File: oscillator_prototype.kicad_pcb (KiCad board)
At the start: 2 copper layers, 99 parts, among them J1 shark fin, J2 Exp FM, J3 1v/oct, J4 Triangle, J5 Pulse, J6 Sync, J7 Eurorack power, J8 Linear FM, J9 PWM, Q1 MMBT3904, Q2 MMBT3906, Q3 BC857BS, Q4 MMBT3904, Q5 MMBT3904, SW1 Sync Mode, SW2 Audio/LFO, U1 LT1013, U2 TL074, U3 LM13700, U4 LM311, U5 LM311, U6 DG418, U7 LM311, U8 TL072

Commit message: Switch to SMT resistors/caps/diodes (mostly)
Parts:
- C1: footprint Capacitor_THT:C_Disc_D5.0mm_W2.5mm_P5.00mm -> Capacitor_SMD:C_0603_1608Metric_Pad1.08x0.95mm_HandSolder
- C10, C11, C12, C13, C14, C15, C16, C17, C19, C20, C21, C22, C23, C24, C25, C26, C3, C4, C5, C7, C8: footprint Capacitor_THT:C_Disc_D5.0mm_W2.5mm_P5.00mm -> Capacitor_SMD:C_0805_2012Metric_Pad1.18x1.45mm_HandSolder
- D1, D2, D3: footprint Diode_THT:D_DO-35_SOD27_P7.62mm_Horizontal -> Diode_SMD:D_0805_2012Metric_Pad1.15x1.40mm_HandSolder
- JP1: moved to B.Cu
- R1, R10, R11, R12, R13, R14, R15, R16, R17, R18, R19, R2, R20, R21, R22, R23, R24, R25, R26, R27, R28, R29, R3, R30, R31, R32, R33, R34, R5, R6, R7, R8, R9: footprint Resistor_THT:R_Axial_DIN0204_L3.6mm_D1.6mm_P5.08mm_Horizontal -> Resistor_SMD:R_0805_2012Metric_Pad1.20x1.40mm_HandSolder
- R4: footprint Resistor_THT:R_Axial_DIN0207_L6.3mm_D2.5mm_P7.62mm_Horizontal -> Resistor_THT:R_Axial_DIN0204_L3.6mm_D1.6mm_P5.08mm_Horizontal
- moved C5 231.3 mm to (46.2, 89.0)
- moved R28 221.7 mm to (55.5, 89.5)
- moved R24 205.7 mm to (50.2, 89.5)
- moved R17 192.4 mm to (97.8, 145.5)
- moved R33 174.4 mm to (99.2, 117.5)
- moved R19 172.7 mm to (92.8, 130.5)
- moved R34 151.3 mm to (107.0, 118.8)
- moved R2 150.5 mm to (116.8, 118.8)
- moved R5 144.8 mm to (117.8, 138.0)
- moved R32 138.1 mm to (112.0, 118.8)
- moved R14 120.0 mm to (150.8, 89.8)
- moved R16 114.9 mm to (118.0, 145.2)
- moved R23 110.0 mm to (138.8, 141.8)
- moved R26 109.7 mm to (166.5, 137.5)
- moved R15 108.0 mm to (163.0, 67.5)
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
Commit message: Complete layout
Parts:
- removed C16, C17, C25, C26, C7, C8: 100n, Capacitor_SMD:C_0805_2012Metric_Pad1.18x1.45mm_HandSolder
- removed J2: Exp FM, kicad_libraries:Jack_3.5mm_QingPu_WQP-PJ398SM_Vertical_CircularHoles-translated
- removed J5: Pulse, kicad_libraries:Jack_3.5mm_QingPu_WQP-PJ398SM_Vertical_CircularHoles-translated
- removed R34: 100k, Resistor_SMD:R_0805_2012Metric_Pad1.20x1.40mm_HandSolder
- removed RV8: B100k, kicad_libraries:Potentiometer_Alpha_RD901F-40-00D_Single_Vertical-translated
- removed RV9: 100k, kicad_libraries:Potentiometer_Alpha_RD901F-40-00D_Single_Vertical-translated
- removed SW2: Audio/LFO, ljwall-kicad-footprints:Dailywell_sub-mini_toggle_DPDT
- added D6: 1N4148, Diode_SMD:D_0805_2012Metric_Pad1.15x1.40mm_HandSolder, F.Cu at (103.0, 115.8)
- added D7: 1N4148, Diode_SMD:D_0805_2012Metric_Pad1.15x1.40mm_HandSolder, F.Cu at (100.8, 115.8)
- added D8: 1N4148, Diode_SMD:D_0805_2012Metric_Pad1.15x1.40mm_HandSolder, F.Cu at (107.8, 106.8)
- added D9: 1N4148, Diode_SMD:D_0805_2012Metric_Pad1.15x1.40mm_HandSolder, F.Cu at (105.5, 106.8)
- added J10: Conn_01x06_Male, Connector_PinHeader_2.54mm:PinHeader_1x06_P2.54mm_Vertical, F.Cu at (97.8, 102.0)
- added J11: Conn_01x06_Female, Connector_PinHeader_2.54mm:PinHeader_1x06_P2.54mm_Vertical, B.Cu at (83.0, 107.0)
- added J12: Conn_01x06_Male, Connector_PinHeader_2.54mm:PinHeader_1x06_P2.54mm_Vertical, F.Cu at (133.0, 107.0)
- added J13: Conn_01x06_Female, Connector_PinHeader_2.54mm:PinHeader_1x06_P2.54mm_Vertical, B.Cu at (47.0, 48.0)
- added J14: Conn_01x06_Male, Connector_PinHeader_2.54mm:PinHeader_1x06_P2.54mm_Vertical, F.Cu at (97.0, 48.0)
- added TP1: vref, TestPoint:TestPoint_Pad_D2.0mm, B.Cu at (109.8, 114.0)
- C1: value C_Small -> 1n; footprint Capacitor_SMD:C_0603_1608Metric_Pad1.08x0.95mm_HandSolder -> Capacitor_SMD:C_0805_2012Metric_Pad1.18x1.45mm_HandSolder
- C5: value 10n -> 100n
- C6: value 470n (polyester) -> 100n; footprint Capacitor_THT:C_Rect_L7.2mm_W3.5mm_P5.00mm_FKS2_FKP2_MKS2_MKP2 -> Capacitor_SMD:C_0805_2012Metric_Pad1.18x1.45mm_HandSolder
- J7: footprint Connector_IDC:IDC-Header_2x05_P2.54mm_Vertical -> Connector_IDC:IDC-Header_2x05_P2.54mm_Horizontal; moved to F.Cu
- J9: value PWM -> Conn_01x06_Female; footprint kicad_libraries:Jack_3.5mm_QingPu_WQP-PJ398SM_Vertical_CircularHoles-translated -> Connector_PinHeader_2.54mm:PinHeader_1x06_P2.54mm_Vertical; moved to B.Cu
- R10, R14: value R_Small_US -> 100k
- R17: value 20k -> 120k
- R19: value 1k -> 3k6
- R24: value 1k -> 10k
- R28: value 1k -> 4k7
- R3: value R_Small_US -> 68k
- R32: value 100k -> 10k
- R33: value 100k -> 4k7
- R6: value R_Small_US -> 680k
- RV1, RV2: value 100k -> 50k
- RV4: value 100k -> 2k; footprint kicad_libraries:Potentiometer_Alpha_RD901F-40-00D_Single_Vertical-translated -> Potentiometer_THT:Potentiometer_Bourns_3266X_Horizontal
- U1: value LT1013 -> LT1013-SOIC
- U5: value LM311 -> LT1013-SOIC
- U8: value TL072 -> LM336Z-5.0; footprint Package_SO:SOIC-8_3.9x4.9mm_P1.27mm -> Package_TO_SOT_THT:TO-92_Inline
- moved C11 143.5 mm to (101.8, 130.5), turned to 270 degrees
- moved C24 139.3 mm to (96.2, 125.8), turned to 90 degrees
- moved C19 127.6 mm to (104.0, 87.0), turned to 90 degrees
- moved C13 119.8 mm to (98.0, 78.0), turned to 270 degrees
- moved C23 116.3 mm to (113.2, 79.0), turned to 180 degrees
- moved C15 112.1 mm to (106.8, 64.0), turned to 90 degrees
- moved U7 111.8 mm to (102.0, 79.8), turned to 90 degrees
- moved C21 109.9 mm to (119.8, 61.2)
- moved D5 109.3 mm to (132.2, 133.2), turned to 90 degrees
- moved D4 107.8 mm to (128.5, 123.0), turned to 270 degrees
- moved R10 104.9 mm to (66.5, 70.2)
- moved C22 102.7 mm to (126.5, 72.8), turned to 270 degrees
- moved C14 101.2 mm to (117.0, 71.0), turned to 180 degrees
- moved U8 101.1 mm to (105.8, 111.5)
- moved D2 100.2 mm to (101.0, 96.2), turned to 270 degrees
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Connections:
- net /SC_b renamed Net-(C4-Pad1)
- C15 pad 1: +12V -> GND
- C15 pad 2: GND -> -12V
- C4 pad 2: /SC_a -> sync_m
- C5 pad 1: Net-(C5-Pad1) -> +12V
- C5 pad 2: /SC_a -> GND
- C6 pad 1: Net-(C6-Pad1) -> +12V
- C6 pad 2: /TC_b -> GND
- J1 pad S: GND -> GND_f
- J1 pad T: Net-(J1-PadT) -> saw_f
- J3 pad S: GND -> GND_f
- J3 pad T: Net-(J3-PadT) -> v_per_oct_f
- J3 pad TN: GND -> GND_f
- J4 pad S: GND -> GND_f
- J4 pad T: Net-(J4-PadT) -> tri_f
- J6 pad S: GND -> GND_f
- J6 pad T: /SC_a -> sync_f
- J6 pad TN: GND -> GND_f
- J8 pad S: GND -> GND_f
- J8 pad TN: GND -> GND_f
- R10 pad 1: Net-(C1-Pad2) -> 5V_f
- R14 pad 2: Net-(J3-PadT) -> v_per_oct_m
- R16 pad 2: Net-(J4-PadT) -> tri_m
- R17 pad 1: Net-(R17-Pad1) -> Net-(C1-Pad2)
- R17 pad 2: +5V -> -5V
- R19 pad 1: Net-(R19-Pad1) -> +12V
- R19 pad 2: Net-(J5-PadT) -> Net-(D6-Pad2)
- R23 pad 1: Net-(R23-Pad1) -> switch_b_m
- R24 pad 1: /SC_a -> Net-(R24-Pad1)
- R24 pad 2: Net-(R24-Pad2) -> -5V
- R28 pad 1: /TC_b -> Net-(D7-Pad1)
- R3 pad 2: Net-(R3-Pad2) -> coarse_m
- R30 pad 1: /TC_b -> /TC_a
- R31 pad 2: Net-(R31-Pad2) -> lin_fm_m
- R32 pad 1: Net-(R32-Pad1) -> Net-(D6-Pad2)
- R32 pad 2: Net-(R32-Pad2) -> Net-(R24-Pad1)
- R33 pad 1: Net-(R32-Pad2) -> Net-(R33-Pad1)
- R5 pad 2: Net-(J1-PadT) -> saw_m
- R6 pad 2: Net-(R6-Pad2) -> fine_m
- RV1 pad 1: -5V -> GND_f
- RV1 pad 2: Net-(R3-Pad2) -> coarse_f
- RV1 pad 3: +5V -> 5V_f
- RV2 pad 1: GND -> GND_f
- RV2 pad 2: Net-(R6-Pad2) -> fine_f
- RV2 pad 3: +5V -> Net-(R10-Pad2)
- RV4 pad 1: Net-(J2-PadT) -> Net-(R33-Pad1)
- RV4 pad 2: Net-(R10-Pad2) -> Net-(RV4-Pad2)
- RV4 pad 3: GND -> Net-(R28-Pad2)
- RV5 pad 1: -5V -> Net-(R20-Pad2)
- RV5 pad 3: Net-(R20-Pad2) -> -5V
- RV7 pad 1: GND -> GND_f
- RV7 pad 2: Net-(R31-Pad2) -> lin_fm_f
- SW1 pad 1: Net-(R23-Pad1) -> switch_b_f
- SW1 pad 2: Net-(SW1-Pad2) -> switch_a_f
- U1 pad 1: Net-(C3-Pad1) -> GND
- U1 pad 2: Net-(C3-Pad2) -> -12V
- U1 pad 4: -12V -> Net-(C3-Pad2)
- U1 pad 5: GND -> Net-(C3-Pad1)
- U1 pad 6: Net-(C1-Pad2) -> +12V
- U1 pad 8: +12V -> Net-(C1-Pad2)
- U2 pad 1: Net-(R32-Pad1) -> Net-(R16-Pad1)
- U2 pad 12: /TC_b -> GND
- U2 pad 13: Net-(R16-Pad1) -> /TC_a
- U2 pad 14: Net-(R16-Pad1) -> /TC_b
- U2 pad 2: Net-(R32-Pad2) -> Net-(R16-Pad1)
- U2 pad 3: GND -> /TC_b
- U2 pad 5: Net-(R17-Pad1) -> GND
- U2 pad 6: Net-(R19-Pad1) -> Net-(U2-Pad6)
- U2 pad 7: Net-(R19-Pad1) -> Net-(U2-Pad6)
- U3 pad 1: Net-(Q2-Pad3) -> Net-(Q3-Pad6)
- U3 pad 10: +12V -> Net-(U3-Pad10)
- U3 pad 12: /TC_a -> Net-(R1-Pad2)
- U3 pad 16: Net-(Q3-Pad6) -> Net-(Q2-Pad3)
- U3 pad 5: Net-(R1-Pad2) -> /TC_a
- U3 pad 7: +12V -> Net-(U3-Pad7)
- U3 pad 8: +12V -> Net-(U3-Pad7)
- U3 pad 9: +12V -> Net-(U3-Pad10)
- U5 pad 1: -5V -> Net-(D6-Pad2)
- U5 pad 2: /TC_b -> -12V
- U5 pad 3: Net-(R32-Pad1) -> GND
- U5 pad 4: -12V -> Net-(R24-Pad1)
- U5 pad 5: Net-(U5-Pad5) -> -5V
- U5 pad 6: Net-(U5-Pad6) -> +12V
- U5 pad 7: Net-(R17-Pad1) -> +5V
- U5 pad 8: +12V -> +5V
- U6 pad 1: /TC_a -> /TC_b
- U6 pad 6: Net-(R23-Pad1) -> switch_b_m
- U7 pad 1: Net-(SW1-Pad2) -> switch_a_m
- U8 pad 1: /TC_b -> Net-(RV4-Pad2)
- U8 pad 2: /TC_a -> Net-(D6-Pad2)
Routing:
- net -12V: track 0.00 -> 270.8 mm, vias 0 -> 8
- net +12V: track 0.00 -> 231.9 mm, vias 0 -> 8
- net +5V: track 0.00 -> 105.5 mm, vias 0 -> 6
- net -5V: track 0.00 -> 103.9 mm, vias 0 -> 4
- net /TC_b: track 0.00 -> 77.3 mm
- net lin_fm_f: track 0.00 -> 76.5 mm, vias 0 -> 2
- net 5V_f: track 0.00 -> 58.8 mm
- net coarse_f: track 0.00 -> 58.6 mm
- net tri_f: track 0.00 -> 54.2 mm, vias 0 -> 4
- net saw_f: track 0.00 -> 49.9 mm, vias 0 -> 4
- net switch_a_f: track 0.00 -> 44.8 mm
- net /TC_a: track 0.00 -> 42.3 mm
- net v_per_oct_f: track 0.00 -> 42.3 mm
- net switch_b_f: track 0.00 -> 39.5 mm
- net Net-(C1-Pad2): track 0.00 -> 35.0 mm, vias 0 -> 1
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- added copper zone on B.Cu, net GND
- added copper zone on F.Cu, net GND
- added copper zone on B.Cu, net GND_f
- added copper zone on F.Cu, net GND_f
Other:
- board outline added: 98.5 x 117 mm
- board text added: "+12V"
- board text added: "-12V"
- board text added: "GND"
- board text added: "Oscillator Prototype 1"
- board text added: "bridge for init trim"
- board text added: "bridge to operate"
- board text added: "hf trim"
- board text added: "init"
- board text added: "red stripe"
- board text added: "v/oct trim"
- board text added: "vref (5v)"
- board text added: "vref trim"

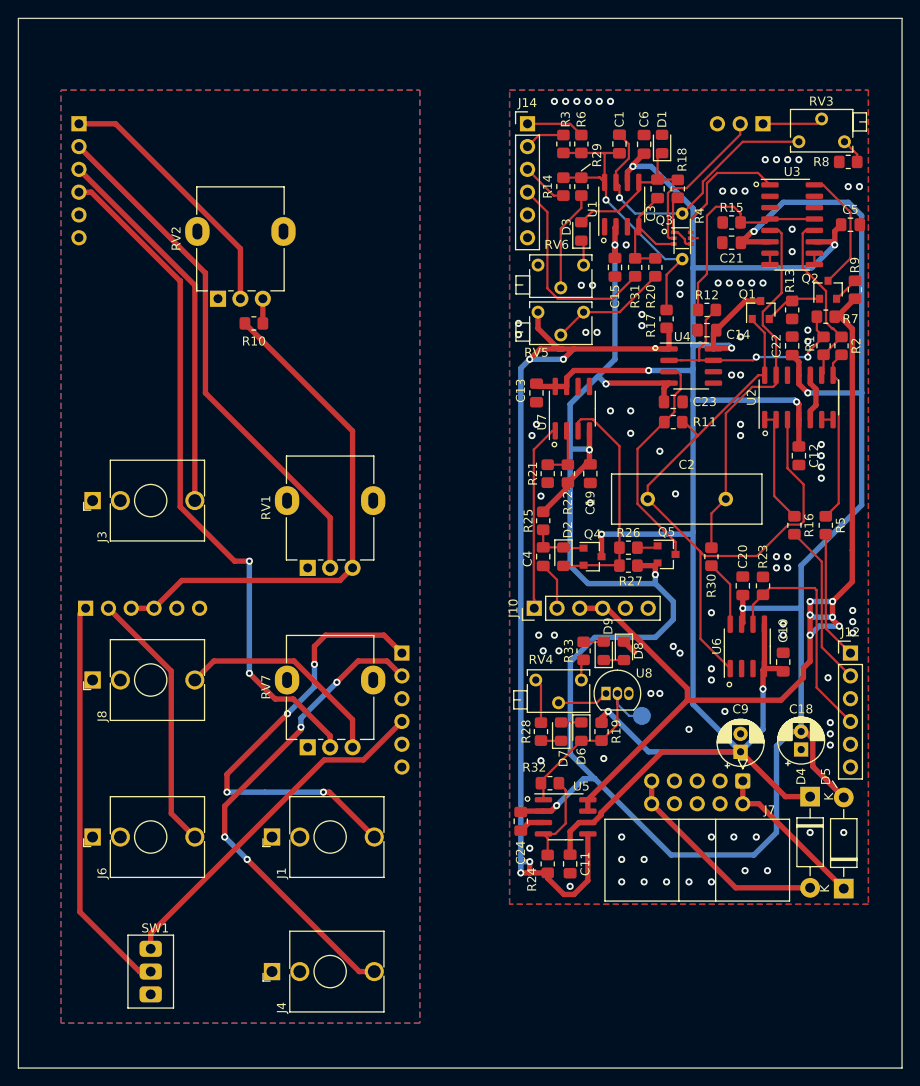
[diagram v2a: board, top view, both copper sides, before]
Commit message: Refactor layout and simplify circuit
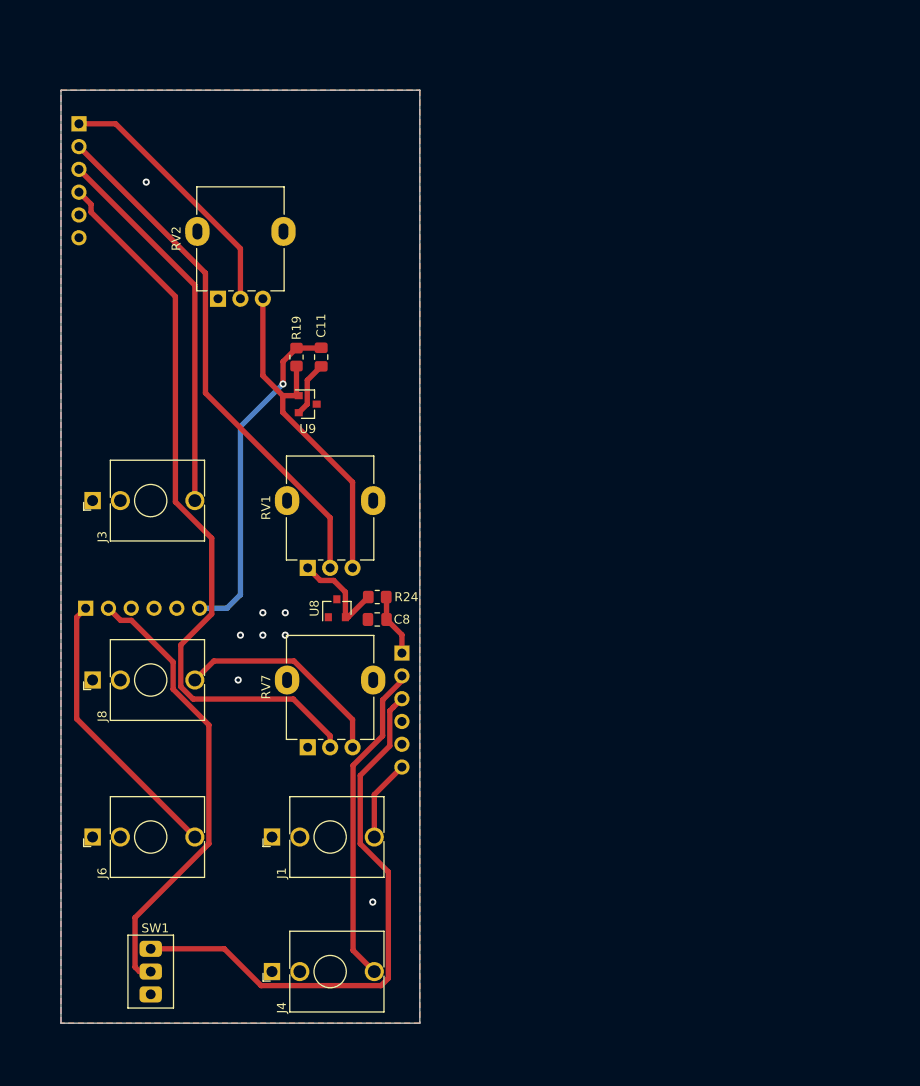
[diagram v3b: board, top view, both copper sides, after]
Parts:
- removed C1: 1n, Capacitor_SMD:C_0805_2012Metric_Pad1.18x1.45mm_HandSolder
- removed C10, C12, C13, C14, C15, C19, C20, C21, C22, C23, C24, C5, C6: 100n, Capacitor_SMD:C_0805_2012Metric_Pad1.18x1.45mm_HandSolder
- removed C18, C9: 4u7, Capacitor_THT:CP_Radial_D5.0mm_P2.00mm
- removed C2: 1n Mica, ljwall-kicad-footprints:Cornell-Dubilier_CD15_Mica_Capacitor_L16.5mm_T5.6mm_P8.7mm
- removed C3: C_Small, Capacitor_SMD:C_0805_2012Metric_Pad1.18x1.45mm_HandSolder
- removed C4: 22p, Capacitor_SMD:C_0805_2012Metric_Pad1.18x1.45mm_HandSolder
- removed D1, D2, D3, D6, D7, D8, D9: 1N4148, Diode_SMD:D_0805_2012Metric_Pad1.15x1.40mm_HandSolder
- removed D4, D5: 1N5818, Diode_THT:D_DO-41_SOD81_P10.16mm_Horizontal
- removed J10, J12, J14: Conn_01x06_Male, Connector_PinHeader_2.54mm:PinHeader_1x06_P2.54mm_Vertical
- removed J7: Eurorack power, Connector_IDC:IDC-Header_2x05_P2.54mm_Horizontal
- removed JP1: Jumper_NC_Dual, Connector_PinHeader_2.54mm:PinHeader_1x03_P2.54mm_Vertical
- removed Q1, Q4, Q5: MMBT3904, Package_TO_SOT_SMD:SOT-23
- removed Q2: MMBT3906, Package_TO_SOT_SMD:SOT-23
- removed Q3: BC857BS, Package_TO_SOT_SMD:SOT-363_SC-70-6
- removed R1: 470k, Resistor_SMD:R_0805_2012Metric_Pad1.20x1.40mm_HandSolder
- removed R10, R12, R14, R27, R9: 100k, Resistor_SMD:R_0805_2012Metric_Pad1.20x1.40mm_HandSolder
- removed R11, R18, R20, R29, R30, R31, R8: R_Small_US, Resistor_SMD:R_0805_2012Metric_Pad1.20x1.40mm_HandSolder
- removed R13, R2, R25: 47k, Resistor_SMD:R_0805_2012Metric_Pad1.20x1.40mm_HandSolder
- removed R15, R21, R26, R7: 20k, Resistor_SMD:R_0805_2012Metric_Pad1.20x1.40mm_HandSolder
- removed R16, R22, R5: 1k, Resistor_SMD:R_0805_2012Metric_Pad1.20x1.40mm_HandSolder
- removed R17: 120k, Resistor_SMD:R_0805_2012Metric_Pad1.20x1.40mm_HandSolder
- removed R23, R32: 10k, Resistor_SMD:R_0805_2012Metric_Pad1.20x1.40mm_HandSolder
- removed R28, R33: 4k7, Resistor_SMD:R_0805_2012Metric_Pad1.20x1.40mm_HandSolder
- removed R3: 68k, Resistor_SMD:R_0805_2012Metric_Pad1.20x1.40mm_HandSolder
- removed R4: Xk yyy ppm, Resistor_THT:R_Axial_DIN0204_L3.6mm_D1.6mm_P5.08mm_Horizontal
- removed R6: 680k, Resistor_SMD:R_0805_2012Metric_Pad1.20x1.40mm_HandSolder
- removed RV3, RV5, RV6: R_POT_TRIM_US, Potentiometer_THT:Potentiometer_Bourns_3266X_Horizontal
- removed RV4: 2k, Potentiometer_THT:Potentiometer_Bourns_3266X_Horizontal
- removed TP1: vref, TestPoint:TestPoint_Pad_D2.0mm
- removed U1, U5: LT1013-SOIC, Package_SO:SOIC-8_3.9x4.9mm_P1.27mm
- removed U2: TL074, Package_SO:SOIC-14_3.9x8.7mm_P1.27mm
- removed U3: LM13700, Package_SO:SOIC-16_3.9x9.9mm_P1.27mm
- removed U4, U7: LM311, Package_SO:SOIC-8_3.9x4.9mm_P1.27mm
- removed U6: DG418, Package_SO:SOIC-8_3.9x4.9mm_P1.27mm
- added C8: 100n, Capacitor_SMD:C_0805_2012Metric_Pad1.18x1.45mm_HandSolder, F.Cu at (80.2, 103.2)
- added U9: LM4040AIM3-2.5, Package_TO_SOT_SMD:SOT-23, F.Cu at (72.5, 79.2)
- R19: value 3k6 -> R_Small_US
- R24: value 10k -> R_Small_US
- U8: value LM336Z-5.0 -> LM4040AIM3-2.5; footprint Package_TO_SOT_THT:TO-92_Inline -> Package_TO_SOT_SMD:SOT-23
- moved C11 62.9 mm to (74.0, 74.0)
- moved R19 53.8 mm to (71.2, 74.0)
- moved R24 35.3 mm to (80.2, 100.8), turned to 0 degrees
- moved U8 31.5 mm to (75.8, 102.0), turned to 90 degrees
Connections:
- C11 pad 1: +12V -> 12V_f
- C11 pad 2: GND -> GND_f
- J11 pad 1: saw_f -> -12V_f
- J11 pad 3: GND_f -> switch_b_f
- J11 pad 4: switch_b_f -> GND_f
- J11 pad 6: GND_f -> saw_f
- J9 pad 1: switch_a_f -> sync_f
- J9 pad 2: sync_f -> switch_a_f
- J9 pad 3: 5V_f -> GND_f
- J9 pad 4: 5V_f -> GND_f
- J9 pad 6: GND_f -> 12V_f
- R19 pad 1: +12V -> 12V_f
- R19 pad 2: Net-(D6-Pad2) -> 2.5V_f
- R24 pad 1: Net-(R24-Pad1) -> -2.5V_f
- R24 pad 2: -5V -> -12V_f
- RV1 pad 1: GND_f -> -2.5V_f
- RV1 pad 3: 5V_f -> 2.5V_f
- RV2 pad 3: Net-(R10-Pad2) -> 2.5V_f
- U8 pad 1: Net-(RV4-Pad2) -> GND_f
- U8 pad 2: Net-(D6-Pad2) -> -2.5V_f
- U8 pad 3: GND -> (no net)
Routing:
- net -12V: track 270.8 -> 0.00 mm, vias 8 -> 0
- net +12V: track 231.9 -> 0.00 mm, vias 8 -> 0
- net +5V: track 105.5 -> 0.00 mm, vias 6 -> 0
- net -5V: track 103.9 -> 0.00 mm, vias 4 -> 0
- net /TC_b: track 77.3 -> 0.00 mm
- net 5V_f: track 58.8 -> 0.00 mm
- net /TC_a: track 42.3 -> 0.00 mm
- net saw_f: track 49.9 -> 9.08 mm, vias 4 -> 0
- net 2.5V_f: track 0.00 -> 39.3 mm
- net 12V_f: track 0.00 -> 38.0 mm, vias 0 -> 1
- net Net-(C1-Pad2): track 35.0 -> 0.00 mm, vias 1 -> 0
- net Net-(C1-Pad1): track 33.0 -> 0.00 mm, vias 1 -> 0
- net Net-(R1-Pad1): track 27.5 -> 0.00 mm, vias 2 -> 0
- net Net-(D2-Pad2): track 26.6 -> 0.00 mm
- net switch_b_m: track 26.3 -> 0.00 mm
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- removed copper zone on B.Cu, net GND
- removed copper zone on F.Cu, net GND
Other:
- board size 98.5 x 117 mm -> 40 x 104 mm
- net class PWR added: clearance 0.2, trace_width 0.6, via_dia 0.8, via_drill 0.4
- board text removed: "+12V"
- board text removed: "-12V"
- board text removed: "GND"
- board text removed: "Oscillator Prototype 1"
- board text removed: "bridge for init trim"
- board text removed: "bridge to operate"
- board text removed: "hf trim"
- board text removed: "init"
- board text removed: "red stripe"
- board text removed: "v/oct trim"
- board text removed: "vref (5v)"
- board text removed: "vref trim"

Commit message: Add gerbers
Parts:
- added C1: 1n, Capacitor_SMD:C_0805_2012Metric_Pad1.18x1.45mm_HandSolder, F.Cu at (107.0, 50.2)
- added C10: 100n, Capacitor_SMD:C_0805_2012Metric_Pad1.18x1.45mm_HandSolder, F.Cu at (121.2, 113.5)
- added C12: 100n, Capacitor_SMD:C_0805_2012Metric_Pad1.18x1.45mm_HandSolder, F.Cu at (122.8, 91.5)
- added C13: 100n, Capacitor_SMD:C_0805_2012Metric_Pad1.18x1.45mm_HandSolder, F.Cu at (109.0, 106.0)
- added C14: 100n, Capacitor_SMD:C_0805_2012Metric_Pad1.18x1.45mm_HandSolder, F.Cu at (104.5, 86.8)
- added C15: 100n, Capacitor_SMD:C_0805_2012Metric_Pad1.18x1.45mm_HandSolder, F.Cu at (106.8, 64.0)
- added C16: 100n, Capacitor_SMD:C_0805_2012Metric_Pad1.18x1.45mm_HandSolder, F.Cu at (132.2, 86.2)
- added C17: 100n, Capacitor_SMD:C_0805_2012Metric_Pad1.18x1.45mm_HandSolder, F.Cu at (105.8, 96.0)
- added C18: 4u7, Capacitor_THT:CP_Radial_D5.0mm_P2.00mm, F.Cu at (127.5, 117.8)
- added C19: 100n, Capacitor_SMD:C_0805_2012Metric_Pad1.18x1.45mm_HandSolder, F.Cu at (100.0, 112.0)
- added C2: 1n C0G, Capacitor_SMD:C_0805_2012Metric_Pad1.18x1.45mm_HandSolder, F.Cu at (117.2, 79.2)
- added C20: 100n, Capacitor_SMD:C_0805_2012Metric_Pad1.18x1.45mm_HandSolder, F.Cu at (119.8, 101.8)
- added C21: 100n, Capacitor_SMD:C_0805_2012Metric_Pad1.18x1.45mm_HandSolder, F.Cu at (121.2, 62.5)
- added C22: 100n, Capacitor_SMD:C_0805_2012Metric_Pad1.18x1.45mm_HandSolder, F.Cu at (120.8, 79.2)
- added C23: 100n, Capacitor_SMD:C_0805_2012Metric_Pad1.18x1.45mm_HandSolder, F.Cu at (110.5, 95.2)
- added C3: C_Small, Capacitor_SMD:C_0805_2012Metric_Pad1.18x1.45mm_HandSolder, F.Cu at (111.5, 55.2)
- added C4: 22p, Capacitor_SMD:C_0805_2012Metric_Pad1.18x1.45mm_HandSolder, F.Cu at (97.2, 116.5)
- added C5: 100n, Capacitor_SMD:C_0805_2012Metric_Pad1.18x1.45mm_HandSolder, F.Cu at (131.5, 62.5)
- added C6: 100n, Capacitor_SMD:C_0805_2012Metric_Pad1.18x1.45mm_HandSolder, F.Cu at (110.0, 50.3)
- added C7: 100n, Capacitor_SMD:C_0805_2012Metric_Pad1.18x1.45mm_HandSolder, F.Cu at (97.2, 84.0)
- added C9: 4u7, Capacitor_THT:CP_Radial_D5.0mm_P2.00mm, F.Cu at (123.2, 125.5)
- added D1: 1N4148, Diode_SMD:D_0805_2012Metric_Pad1.15x1.40mm_HandSolder, F.Cu at (112.0, 50.2)
- added D2: 1N4148, Diode_SMD:D_0805_2012Metric_Pad1.15x1.40mm_HandSolder, F.Cu at (101.8, 116.5)
- added D3: 1N4148, Diode_SMD:D_0805_2012Metric_Pad1.15x1.40mm_HandSolder, F.Cu at (103.0, 60.0)
- added D4: 1N5818, Diode_THT:D_DO-41_SOD81_P10.16mm_Horizontal, F.Cu at (128.5, 123.0)
- added D5: 1N5818, Diode_THT:D_DO-41_SOD81_P10.16mm_Horizontal, F.Cu at (132.2, 133.2)
- added J10: Conn_01x06_Male, Connector_PinHeader_2.54mm:PinHeader_1x06_P2.54mm_Vertical, F.Cu at (97.8, 102.0)
- added J12: Conn_01x06_Male, Connector_PinHeader_2.54mm:PinHeader_1x06_P2.54mm_Vertical, F.Cu at (133.0, 107.0)
- added J14: Conn_01x06_Male, Connector_PinHeader_2.54mm:PinHeader_1x06_P2.54mm_Vertical, F.Cu at (97.0, 48.0)
- added J7: Eurorack power, Connector_IDC:IDC-Header_2x05_P2.54mm_Horizontal, F.Cu at (113.5, 121.2)
- added Q1: MMBT3904, Package_TO_SOT_SMD:SOT-23, F.Cu at (116.0, 74.2)
- added Q2: MMBT3906, Package_TO_SOT_SMD:SOT-23, F.Cu at (128.0, 68.8)
- added Q3: BC857BS, Package_TO_SOT_SMD:SOT-363_SC-70-6, F.Cu at (114.2, 60.8)
- added Q4: MMBT3904, Package_TO_SOT_SMD:SOT-23, F.Cu at (105.0, 116.5)
- added Q5: MMBT3904, Package_TO_SOT_SMD:SOT-23, F.Cu at (113.2, 116.2)
- added R1: 470k, Resistor_SMD:R_0805_2012Metric_Pad1.20x1.40mm_HandSolder, F.Cu at (124.2, 79.2)
- added R11: R_Small_US, Resistor_SMD:R_0805_2012Metric_Pad1.20x1.40mm_HandSolder, F.Cu at (116.5, 101.8)
- added R12: 100k, Resistor_SMD:R_0805_2012Metric_Pad1.20x1.40mm_HandSolder, F.Cu at (121.8, 74.2)
- added R13: 47k, Resistor_SMD:R_0805_2012Metric_Pad1.20x1.40mm_HandSolder, F.Cu at (119.5, 74.2)
- added R14: 100k, Resistor_SMD:R_0805_2012Metric_Pad1.20x1.40mm_HandSolder, F.Cu at (101.0, 55.0)
- added R15: 20k, Resistor_SMD:R_0805_2012Metric_Pad1.20x1.40mm_HandSolder, F.Cu at (121.2, 57.5)
- added R16: 1k, Resistor_SMD:R_0805_2012Metric_Pad1.20x1.40mm_HandSolder, F.Cu at (120.2, 91.5)
- added R17: R_Small_US, Resistor_SMD:R_0805_2012Metric_Pad1.20x1.40mm_HandSolder, F.Cu at (99.5, 84.0)
- added R18: R_Small_US, Resistor_SMD:R_0805_2012Metric_Pad1.20x1.40mm_HandSolder, F.Cu at (113.8, 55.2)
- added R2: 47k, Resistor_SMD:R_0805_2012Metric_Pad1.20x1.40mm_HandSolder, F.Cu at (126.2, 79.2)
- added R20: R_Small_US, Resistor_SMD:R_0805_2012Metric_Pad1.20x1.40mm_HandSolder, F.Cu at (111.2, 64.0)
- added R21: 20k, Resistor_SMD:R_0805_2012Metric_Pad1.20x1.40mm_HandSolder, F.Cu at (100.0, 107.2)
- added R22: 1k, Resistor_SMD:R_0805_2012Metric_Pad1.20x1.40mm_HandSolder, F.Cu at (100.0, 109.5)
- added R23: 10k, Resistor_SMD:R_0805_2012Metric_Pad1.20x1.40mm_HandSolder, F.Cu at (122.0, 101.8)
- added R25: 47k, Resistor_SMD:R_0805_2012Metric_Pad1.20x1.40mm_HandSolder, F.Cu at (99.5, 116.5)
- added R26: 20k, Resistor_SMD:R_0805_2012Metric_Pad1.20x1.40mm_HandSolder, F.Cu at (109.0, 115.5)
- added R27: 100k, Resistor_SMD:R_0805_2012Metric_Pad1.20x1.40mm_HandSolder, F.Cu at (109.0, 117.5)
- added R28: R_Small_US, Resistor_SMD:R_0805_2012Metric_Pad1.20x1.40mm_HandSolder, F.Cu at (130.0, 86.2)
- added R29: R_Small_US, Resistor_SMD:R_0805_2012Metric_Pad1.20x1.40mm_HandSolder, F.Cu at (103.0, 55.0)
- added R3: ??k, Resistor_SMD:R_0805_2012Metric_Pad1.20x1.40mm_HandSolder, F.Cu at (101.0, 50.2)
- added R30: R_Small_US, Resistor_SMD:R_0805_2012Metric_Pad1.20x1.40mm_HandSolder, F.Cu at (118.0, 91.5)
- added R31: R_Small_US, Resistor_SMD:R_0805_2012Metric_Pad1.20x1.40mm_HandSolder, F.Cu at (109.0, 64.0)
- added R32: R_Small_US, Resistor_SMD:R_0805_2012Metric_Pad1.20x1.40mm_HandSolder, F.Cu at (102.2, 96.0)
- added R4: Xk yyy ppm, Resistor_THT:R_Axial_DIN0204_L3.6mm_D1.6mm_P5.08mm_Horizontal, F.Cu at (114.2, 58.0)
- added R5: 1k, Resistor_SMD:R_0805_2012Metric_Pad1.20x1.40mm_HandSolder, F.Cu at (127.8, 86.2)
- added R6: ??k, Resistor_SMD:R_0805_2012Metric_Pad1.20x1.40mm_HandSolder, F.Cu at (103.0, 50.2)
- added R7: 20k, Resistor_SMD:R_0805_2012Metric_Pad1.20x1.40mm_HandSolder, F.Cu at (125.5, 74.2)
- added R8: R_Small_US, Resistor_SMD:R_0805_2012Metric_Pad1.20x1.40mm_HandSolder, F.Cu at (132.8, 52.2)
- added R9: 100k, Resistor_SMD:R_0805_2012Metric_Pad1.20x1.40mm_HandSolder, F.Cu at (128.0, 74.2)
- added RV3: R_POT_TRIM_US, Potentiometer_THT:Potentiometer_Bourns_3266X_Horizontal, F.Cu at (127.2, 50.0)
- added RV6: R_POT_TRIM_US, Potentiometer_THT:Potentiometer_Bourns_3266X_Horizontal, F.Cu at (103.2, 67.5)
- added TP1: TestPoint, TestPoint:TestPoint_Pad_2.5x2.5mm, B.Cu at (116.8, 49.5)
- added U1: LT1013-SOIC, Package_SO:SOIC-8_3.9x4.9mm_P1.27mm, F.Cu at (107.5, 57.0)
- added U10: LM4040AIM3-5, Package_TO_SOT_SMD:SOT-23, F.Cu at (131.0, 79.5)
- added U11: LM4040AIM3-5, Package_TO_SOT_SMD:SOT-23, F.Cu at (102.2, 91.2)
- added U2: TL074, Package_SO:SOIC-14_3.9x8.7mm_P1.27mm, F.Cu at (121.5, 85.0)
- added U3: LM13700, Package_SO:SOIC-16_3.9x9.9mm_P1.27mm, F.Cu at (126.5, 59.2)
- added U4: LM311, Package_SO:SOIC-8_3.9x4.9mm_P1.27mm, F.Cu at (108.5, 89.2)
- added U5: LM4040AIM3-2.5, Package_TO_SOT_SMD:SOT-23, F.Cu at (98.0, 79.8)
- added U6: DG418, Package_SO:SOIC-8_3.9x4.9mm_P1.27mm, F.Cu at (120.2, 108.5)
- added U7: LM311, Package_SO:SOIC-8_3.9x4.9mm_P1.27mm, F.Cu at (107.2, 110.0)
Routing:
- net -12V: track 0.00 -> 300.2 mm, vias 0 -> 8
- net +12V: track 0.00 -> 251.0 mm
- net /TC_b: track 0.00 -> 44.1 mm
- net /TC_a: track 0.00 -> 40.7 mm
- net Net-(C1-Pad1): track 0.00 -> 37.4 mm, vias 0 -> 2
- net saw_m: track 0.00 -> 37.1 mm, vias 0 -> 2
- net Net-(R1-Pad1): track 0.00 -> 35.2 mm, vias 0 -> 2
- net /soft_sync_pull_down: track 0.00 -> 32.9 mm, vias 0 -> 2
- net Net-(D4-Pad2): track 0.00 -> 31.6 mm
- net Net-(R1-Pad2): track 0.00 -> 29.6 mm
- net Net-(C1-Pad2): track 0.00 -> 28.9 mm, vias 0 -> 1
- net lin_fm_m: track 0.00 -> 28.2 mm
- net Net-(Q3-Pad2): track 0.00 -> 28.2 mm, vias 0 -> 1
- net GND: track 0.00 -> 27.9 mm, vias 0 -> 46
- net Net-(D5-Pad1): track 0.00 -> 25.2 mm
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- added copper zone on B.Cu, net GND
- added copper zone on F.Cu, net GND
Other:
- board size 40 x 104 mm -> 90 x 104 mm
- board text added: "+12V"
- board text added: "-12V"
- board text added: "GND"
- board text added: "Oscillator Prototype 1"
- board text added: "hf trim"
- board text added: "red stripe"
- board text added: "v/oct trim"
